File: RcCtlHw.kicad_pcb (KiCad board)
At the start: 2 copper layers, 26.7 x 42.5 mm, 28 parts, among them J1 USB_B_Mini, J2 Program, J3 TFT_LCD, SW1 On/Off, U1 TP4056, U2 ESP-M2, U3 ADS1015, U4 Joystick

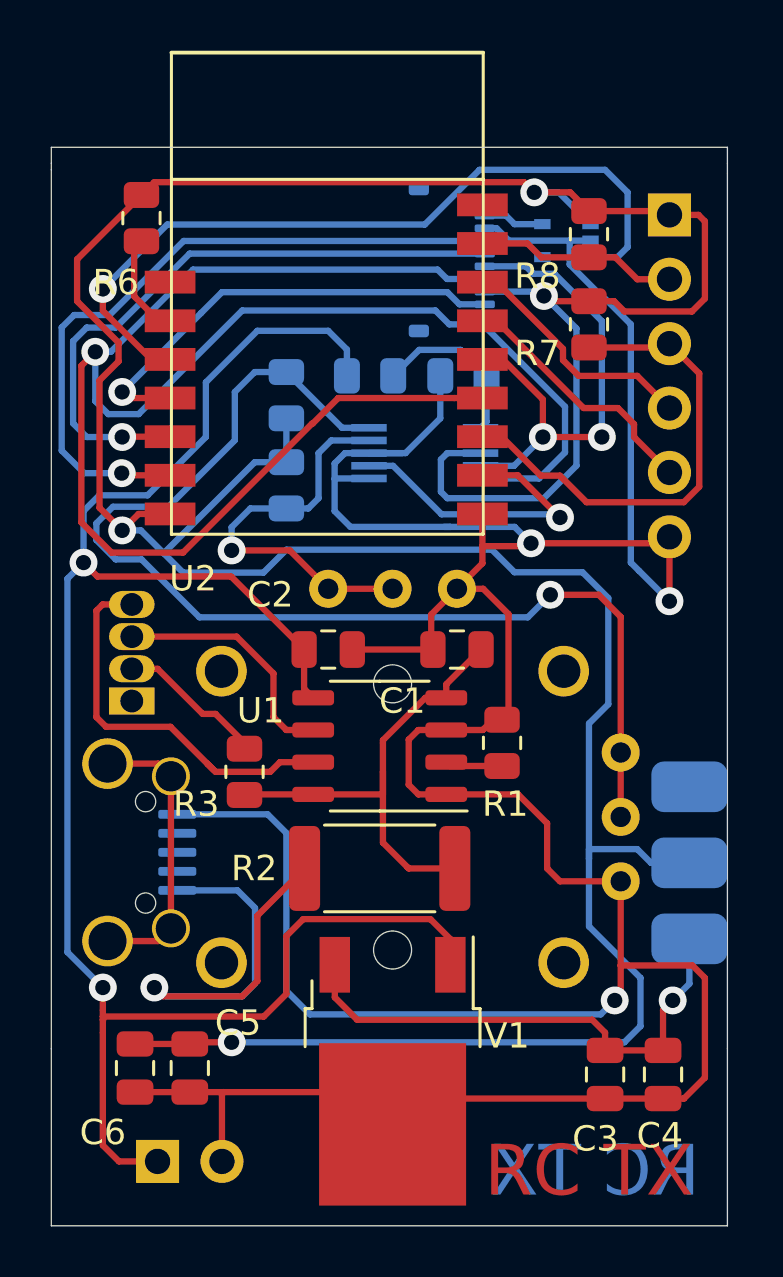
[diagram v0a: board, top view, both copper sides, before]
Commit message: Re-Design with big changes for TFT connection
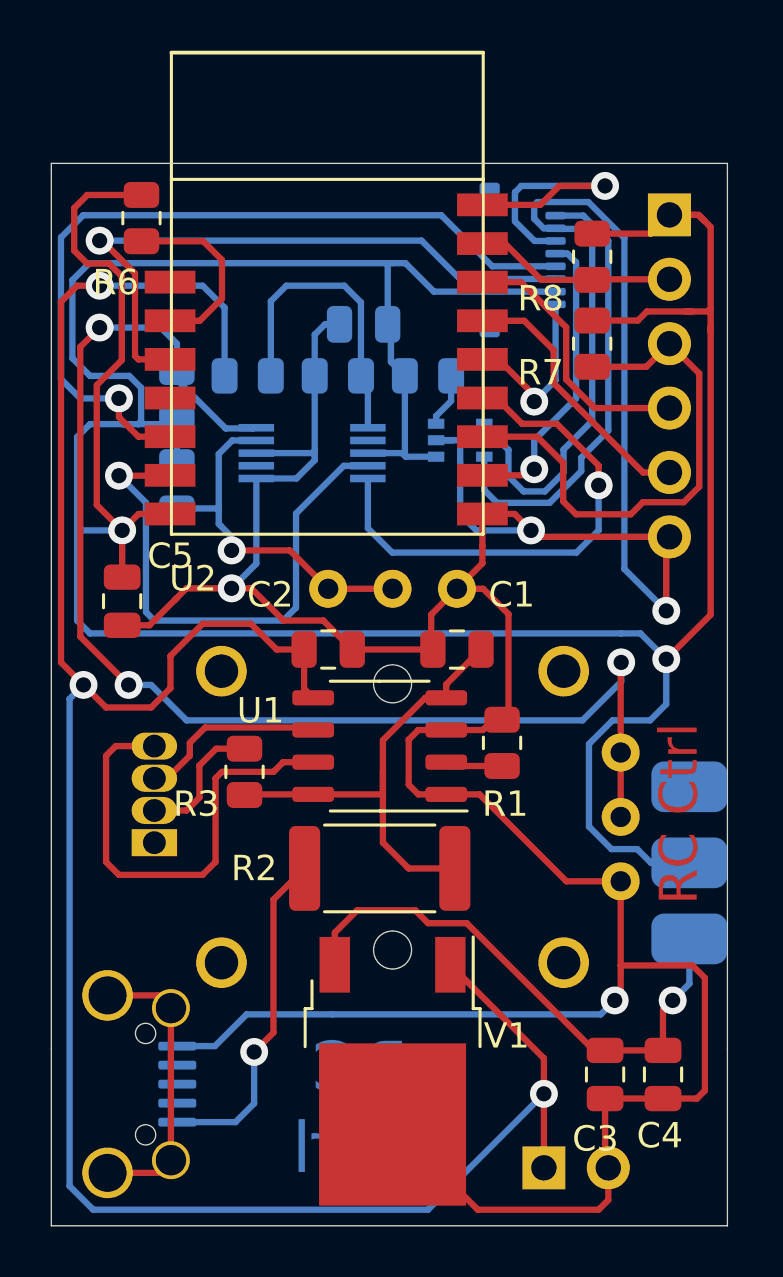
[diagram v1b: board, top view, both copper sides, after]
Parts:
- added R11: 10K, Resistor_SMD:R_0805_2012Metric, B.Cu at (129.2, 92.8)
- C6: moved to B.Cu
- V1: value Regulator -> 3V3
- moved C6 30.7 mm to (126.6, 90.8), turned to 180 degrees
- moved C5 18.6 mm to (117.1, 101.7)
- moved BT1 15.2 mm to (133.7, 124.1)
- moved J1 9.14 mm to (112.3, 120.8)
- moved V2 8.92 mm to (130.4, 95.4), turned to 0 degrees
- moved D1 5.66 mm to (118.4, 111.3)
- moved R10 4.95 mm to (125.6, 92.8)
- moved R9 4.83 mm to (122.0, 92.8)
- moved U3 4.45 mm to (124.6, 95.9)
- moved R4 4.32 mm to (119.3, 93.6)
- moved R5 4.32 mm to (119.3, 97.2)
- moved J3 2.79 mm to (131.2, 88.3)
- moved R8 0.90 mm to (135.6, 88.1)
- moved R7 0.77 mm to (135.6, 91.6)
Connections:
- U2 pad 11: /SCL -> /I2C_SCL
- U2 pad 12: /SDA -> /TFT_CS
- U2 pad 16: (no net) -> /TFT_RST
- U2 pad 3: Net-(U2-Pad3) -> /SCL
- U2 pad 4: /TFT_CS -> (no net)
- U2 pad 5: /TFT_RS -> /SDA
- U2 pad 6: /TFT_RST -> /I2C_SDA
- U2 pad 9: Net-(U2-Pad9) -> /TFT_RS
- U3 pad 10: /SCL -> /I2C_SCL
- U3 pad 2: Net-(U2-Pad9) -> (no net)
- U3 pad 9: /SDA -> /I2C_SDA
- V2 pad 3: Net-(U2-Pad3) -> Net-(R11-Pad2)
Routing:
- net /SCL: track 72.2 -> 25.2 mm
- net Net-(U2-Pad3): track 31.1 -> 0.00 mm, vias 1 -> 0
- net /I2C_SDA: track 0.00 -> 21.4 mm, vias 0 -> 1
- net /I2C_SCL: track 0.00 -> 20.1 mm, vias 0 -> 1
- net GND: track 146.4 -> 164.2 mm, vias 3 -> 4
- net /TFT_RST: track 27.6 -> 11.9 mm
- net /2V8_BackLight: track 2.41 -> 17.9 mm
- net +BATT: track 74.5 -> 89.6 mm, vias 2 -> 3
- net /TFT_RS: track 25.0 -> 11.9 mm
- net Net-(U2-Pad9): track 12.1 -> 0.00 mm, vias 1 -> 0
- net /SDA: track 19.9 -> 32.0 mm, vias 2 -> 1
- net /TFT_CS: track 18.1 -> 7.07 mm
- net Net-(J1-Pad1): track 20.3 -> 13.4 mm
- net Net-(R10-Pad1): track 6.68 -> 12.1 mm
- net Net-(R4-Pad2): track 46.5 -> 51.4 mm, vias 1 -> 3
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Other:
- board size 26.7 x 42.5 mm -> 26.7 x 41.9 mm
- board text added: "Ctrl"
- board text added: "RC"
- board text added: "RC Ctrl"
- board text removed: "RC TX"

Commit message: TFT_CS now connected GND, GPIO5 back to I2C_SDA PCB linked, mostly working USB connector beefed
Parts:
- V1: value 3V3 -> Regulator
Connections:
- net /SCL renamed /TFT_SCL
- net /SDA renamed /TFT_SDA
- J3 pad 8: /TFT_CS -> GND
- U2 pad 12: /TFT_CS -> /I2C_SDA
- U2 pad 6: /I2C_SDA -> (no net)
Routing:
- net GND: track 164.2 -> 153.8 mm, vias 4 -> 3
- net /Flash: track 20.7 -> 30.3 mm
- net /TFT_CS: track 7.07 -> 0.00 mm, vias 1 -> 0
- net +BATT: track 89.6 -> 85.6 mm
- net +3V3: track 142.1 -> 144.9 mm
- net /2V8_BackLight: track 17.9 -> 20.5 mm
- net /TFT_RS: track 11.9 -> 13.9 mm
- net /I2C_SDA: track 21.4 -> 20.2 mm
- net Net-(C3-Pad1): track 21.7 -> 22.6 mm
- net Net-(J1-Pad1): track 13.4 -> 14.0 mm
- net Net-(R6-Pad2): track 7.41 -> 7.93 mm

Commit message: beefed up USB connector mountings, joystick now swings GND to 3V3 on H & V
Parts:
- removed R4, R5: 10K, Resistor_SMD:R_0805_2012Metric
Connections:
- U3 pad 4: Net-(R5-Pad2) -> Net-(U3-Pad4)
- U3 pad 5: Net-(R4-Pad2) -> Net-(U3-Pad5)
- U4 pad 1: Net-(R5-Pad2) -> +3V3
- U4 pad 2: Net-(R5-Pad2) -> Net-(U3-Pad4)
- U4 pad 4: Net-(R4-Pad2) -> +3V3
- U4 pad 5: Net-(R4-Pad2) -> Net-(U3-Pad5)
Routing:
- net Net-(U3-Pad5): track 0.00 -> 52.0 mm, vias 0 -> 3
- net Net-(R4-Pad2): track 51.2 -> 0.00 mm, vias 3 -> 0
- net Net-(R5-Pad2): track 14.4 -> 0.00 mm, vias 1 -> 0
- net Net-(U3-Pad4): track 0.00 -> 12.8 mm, vias 0 -> 1
- net +3V3: track 144.9 -> 154.5 mm
- net Net-(J1-Pad6): track 11.4 -> 18.4 mm

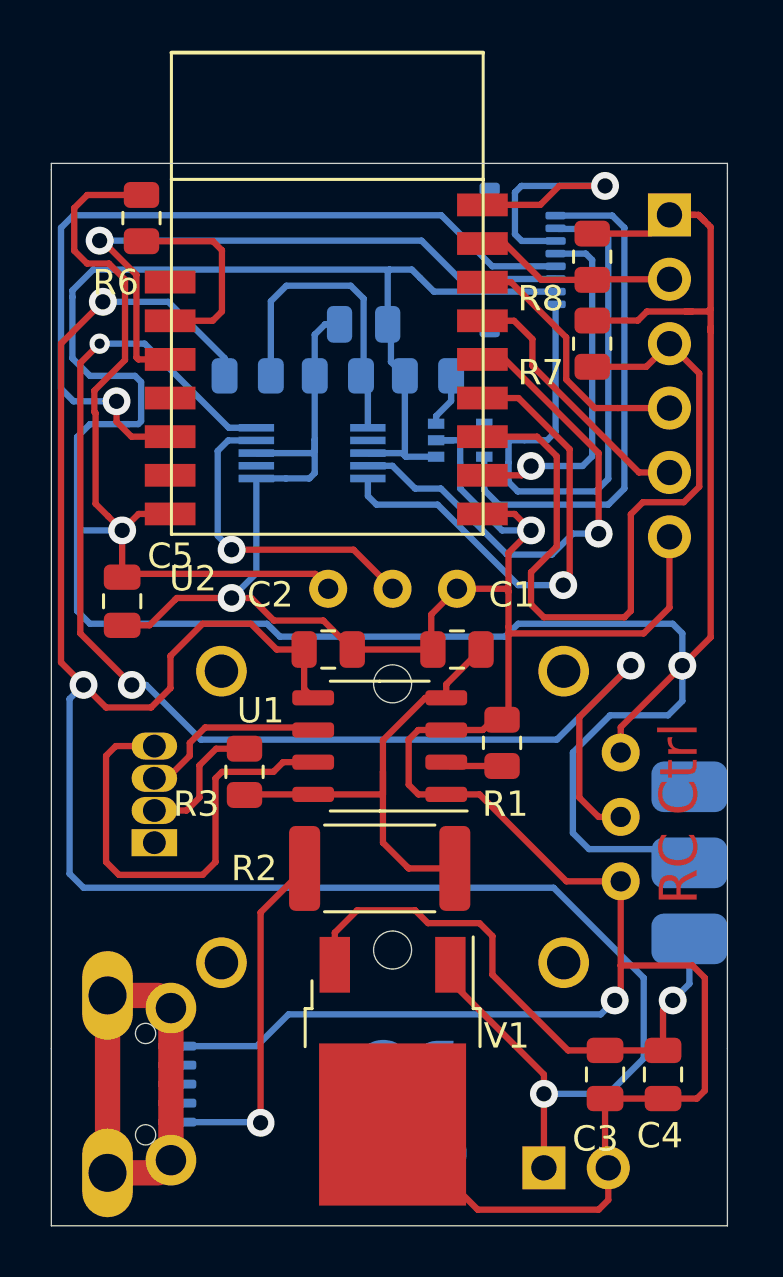
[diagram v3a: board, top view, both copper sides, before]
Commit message: Re-worked USB connector and Joystick to allow oval holes for legs Cleaned up tracks
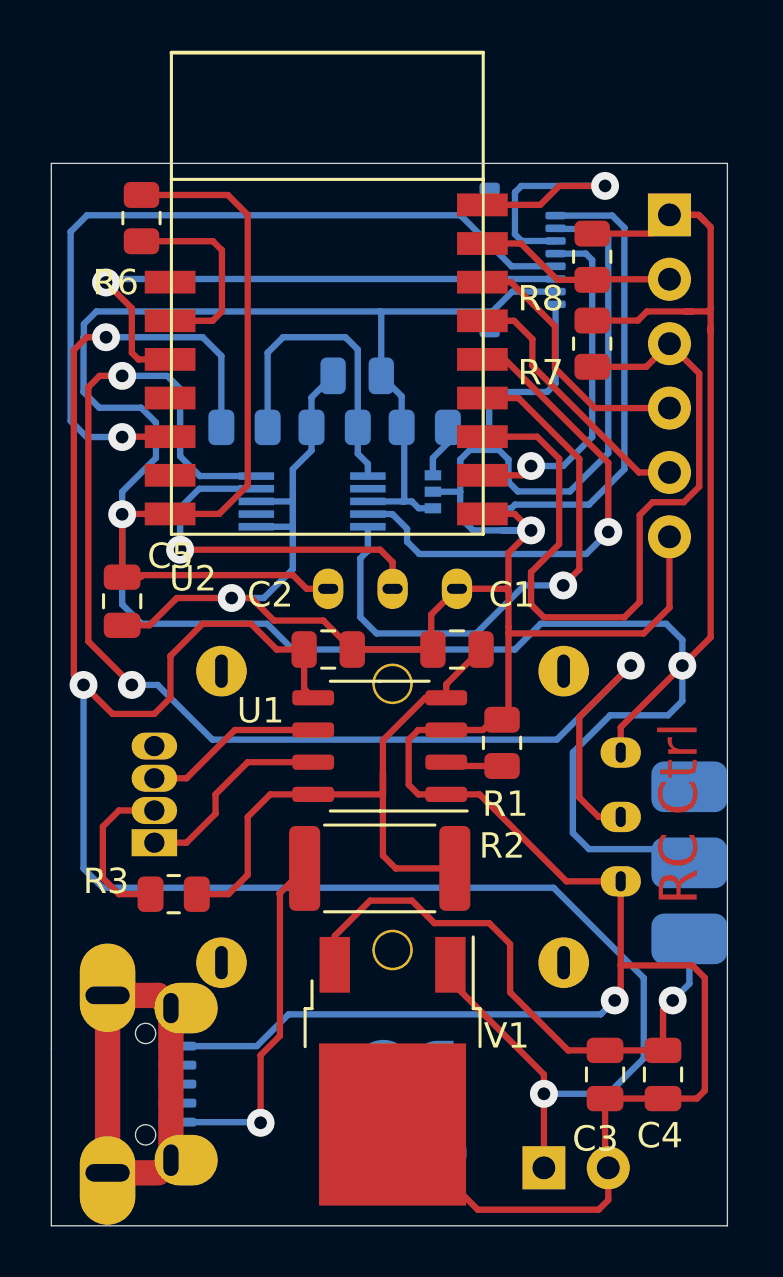
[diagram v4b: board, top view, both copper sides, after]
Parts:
- V1: value Regulator -> 3V3
- moved R3 5.58 mm to (119.1, 113.3), turned to 0 degrees
- moved C6 2.05 mm to (126.4, 92.8)
- moved V2 2.04 mm to (130.3, 97.4)
- moved R10 2.04 mm to (125.5, 94.9)
- moved R9 2.04 mm to (121.9, 94.9)
- moved R11 2.04 mm to (129.0, 94.9)
- moved U3 1.91 mm to (124.6, 97.8)
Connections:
- D1 pad 1: (no net) -> Net-(D1-Pad1)
- D1 pad 4: Net-(D1-Pad4) -> (no net)
- U1 pad 7: Net-(D1-Pad4) -> Net-(D1-Pad1)
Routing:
- net Net-(D1-Pad4): track 18.4 -> 0.00 mm
- net Net-(D1-Pad1): track 0.00 -> 8.03 mm
- net +3V3: track 154.5 -> 148.4 mm
- net Net-(C1-Pad1): track 19.3 -> 24.5 mm
- net /I2C_SCL: track 19.6 -> 22.8 mm
- net /TFT_SCL: track 25.2 -> 22.6 mm
- net GND: track 153.8 -> 151.3 mm
- net /2V8_BackLight: track 20.5 -> 18.7 mm
- net Net-(U3-Pad4): track 12.8 -> 14.6 mm
- net Net-(D1-Pad2): track 5.31 -> 6.47 mm
- net /TFT_SDA: track 32.5 -> 31.9 mm
- net +BATT: track 85.6 -> 85.1 mm

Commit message: Playing 3D, no real change
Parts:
- D1: footprint LED_THT:LED_D5.0mm-4_RGB -> TrevM:LED_D5.0mm-4_RGB-RIGHT
- V1: value 3V3 -> Regulator

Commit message: More 3D play
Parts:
- J2: footprint Connector_PinHeader_2.54mm:PinHeader_1x06_P2.54mm_Vertical -> TrevM:PinHeader_1x06_P2.54mm_Vertical_bent

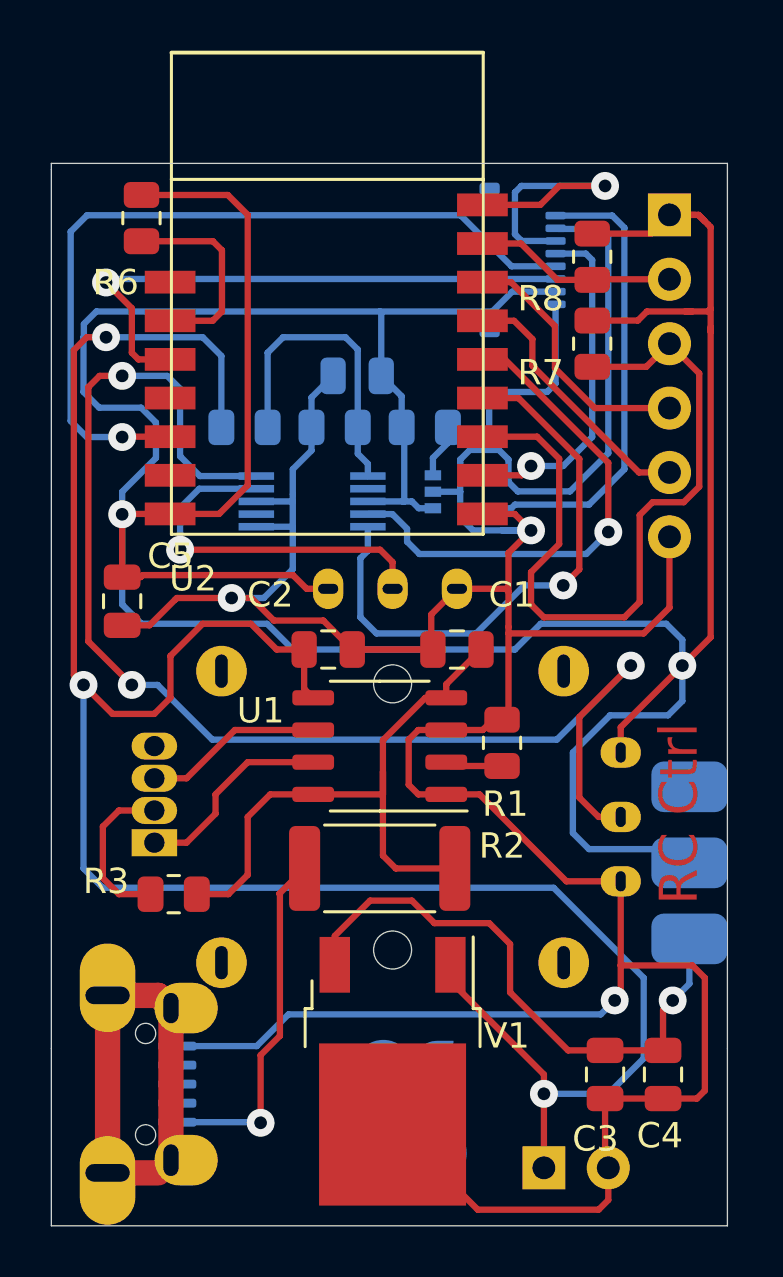
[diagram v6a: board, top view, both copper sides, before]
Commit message: Added 100n capacitors to ADCs
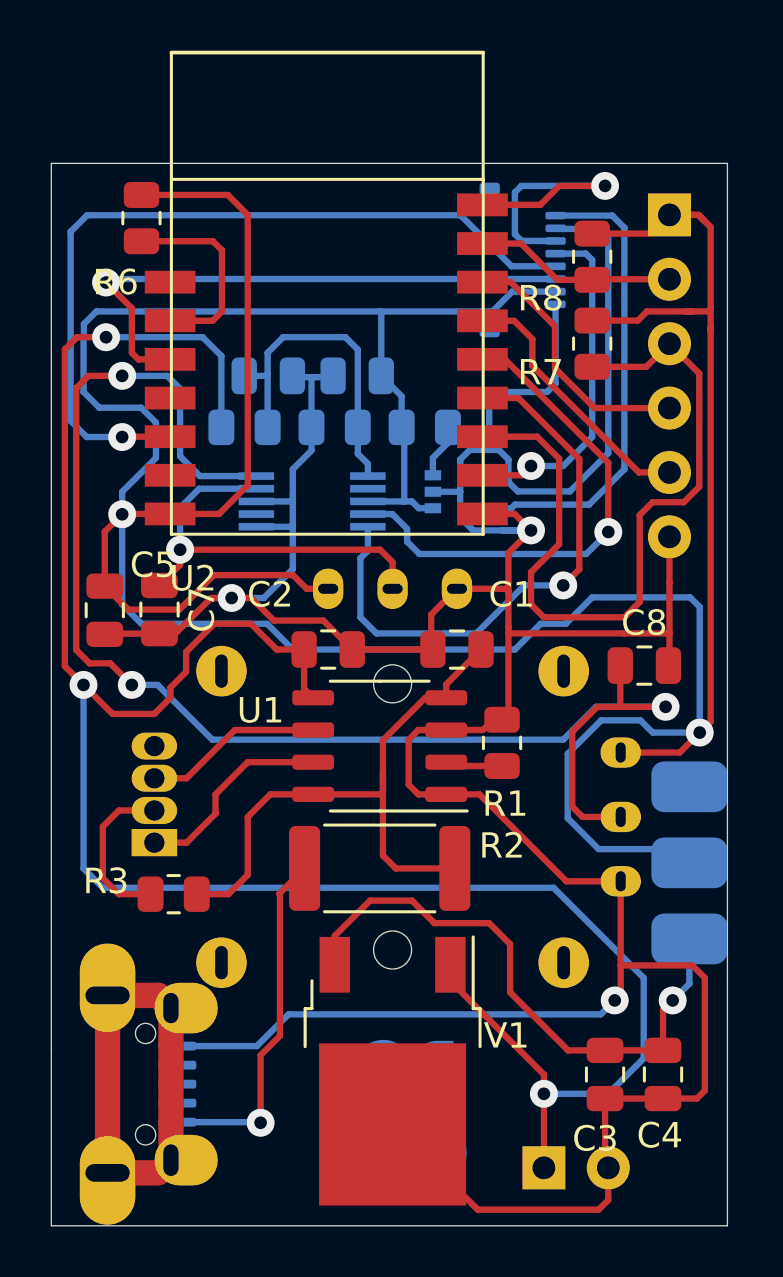
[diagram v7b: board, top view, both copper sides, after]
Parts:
- added C7: 100n, Capacitor_SMD:C_0805_2012Metric, F.Cu at (118.6, 102.1)
- added C8: 100n, Capacitor_SMD:C_0805_2012Metric, F.Cu at (137.7, 104.3)
- added C9: 100n, Capacitor_SMD:C_0805_2012Metric, B.Cu at (122.9, 92.8)
- C5, C6: value u1 -> 100n
- moved C5 0.77 mm to (116.4, 102.1)
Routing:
- net +3V3: track 148.4 -> 156.1 mm
- net Net-(C8-Pad1): track 52.3 -> 56.8 mm
- net GND: track 151.3 -> 155.2 mm
- net Net-(C7-Pad1): track 14.6 -> 16.4 mm
- net Net-(C9-Pad1): track 12.1 -> 13.1 mm
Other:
- board text removed: "RC Ctrl"
